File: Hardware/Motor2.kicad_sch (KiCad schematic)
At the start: 36 parts

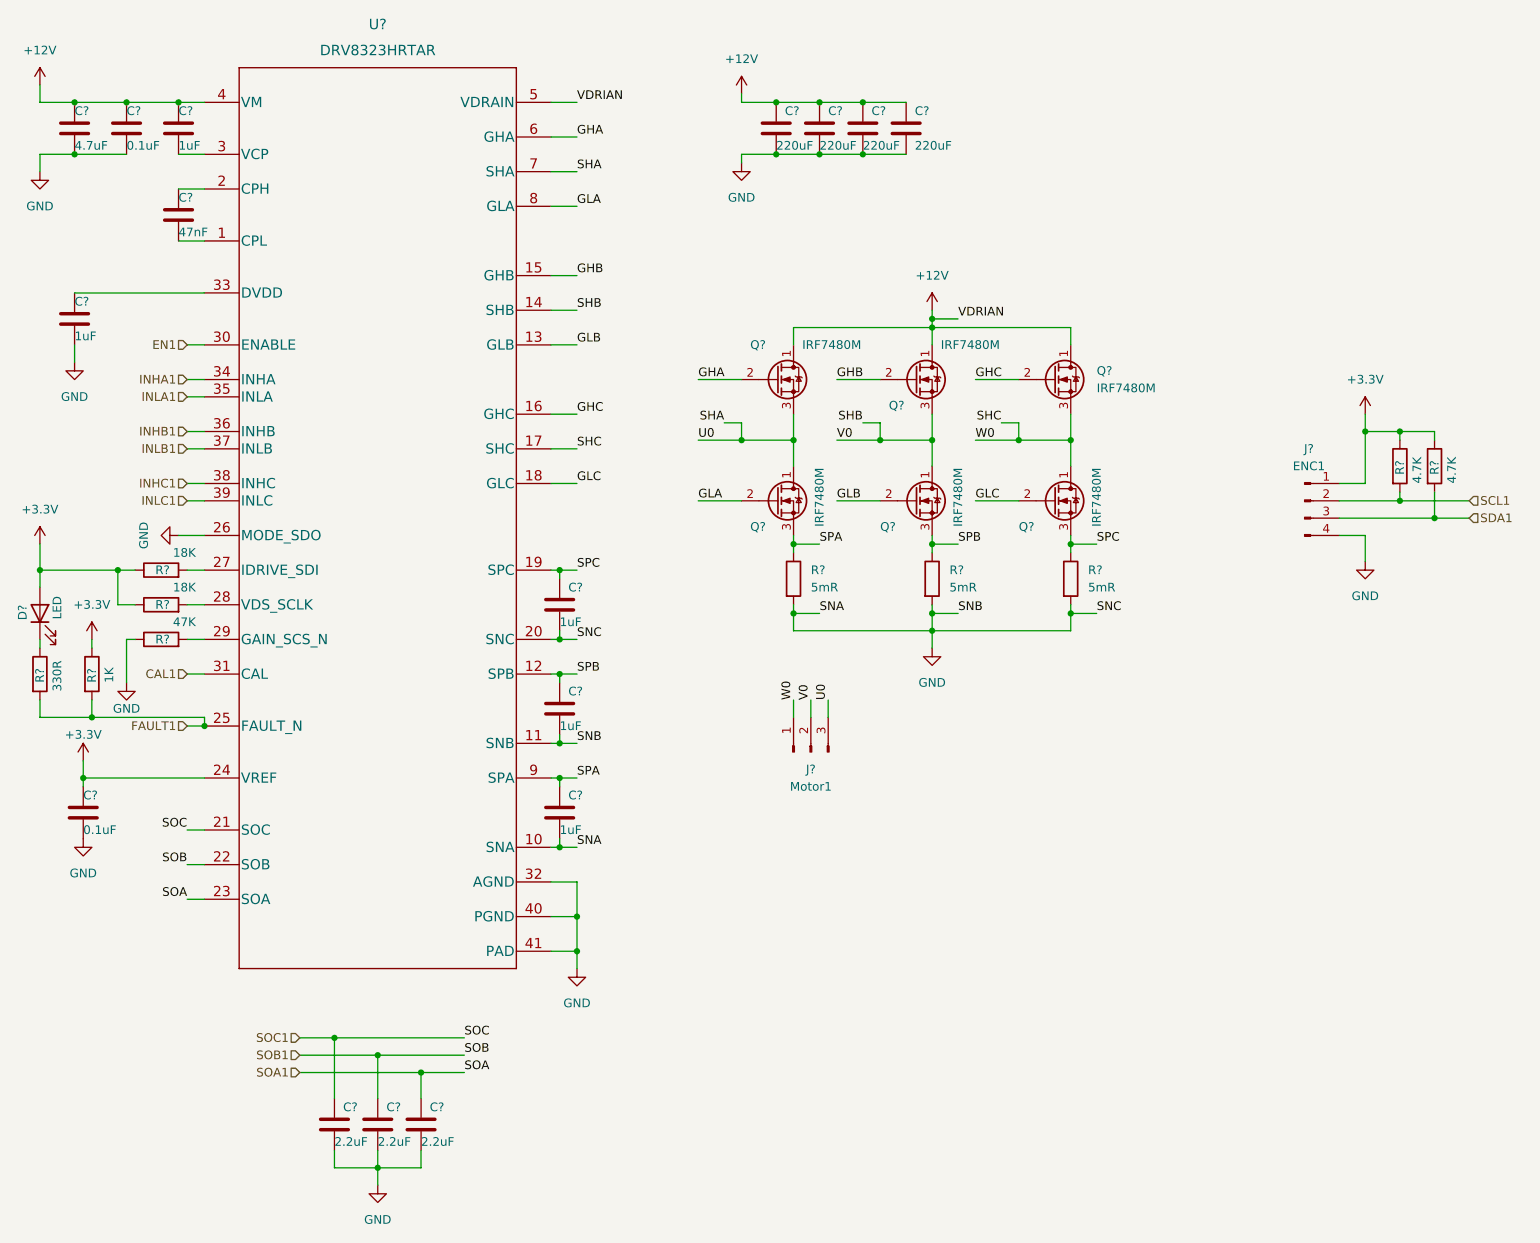
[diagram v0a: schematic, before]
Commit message: Init FreeRTOS
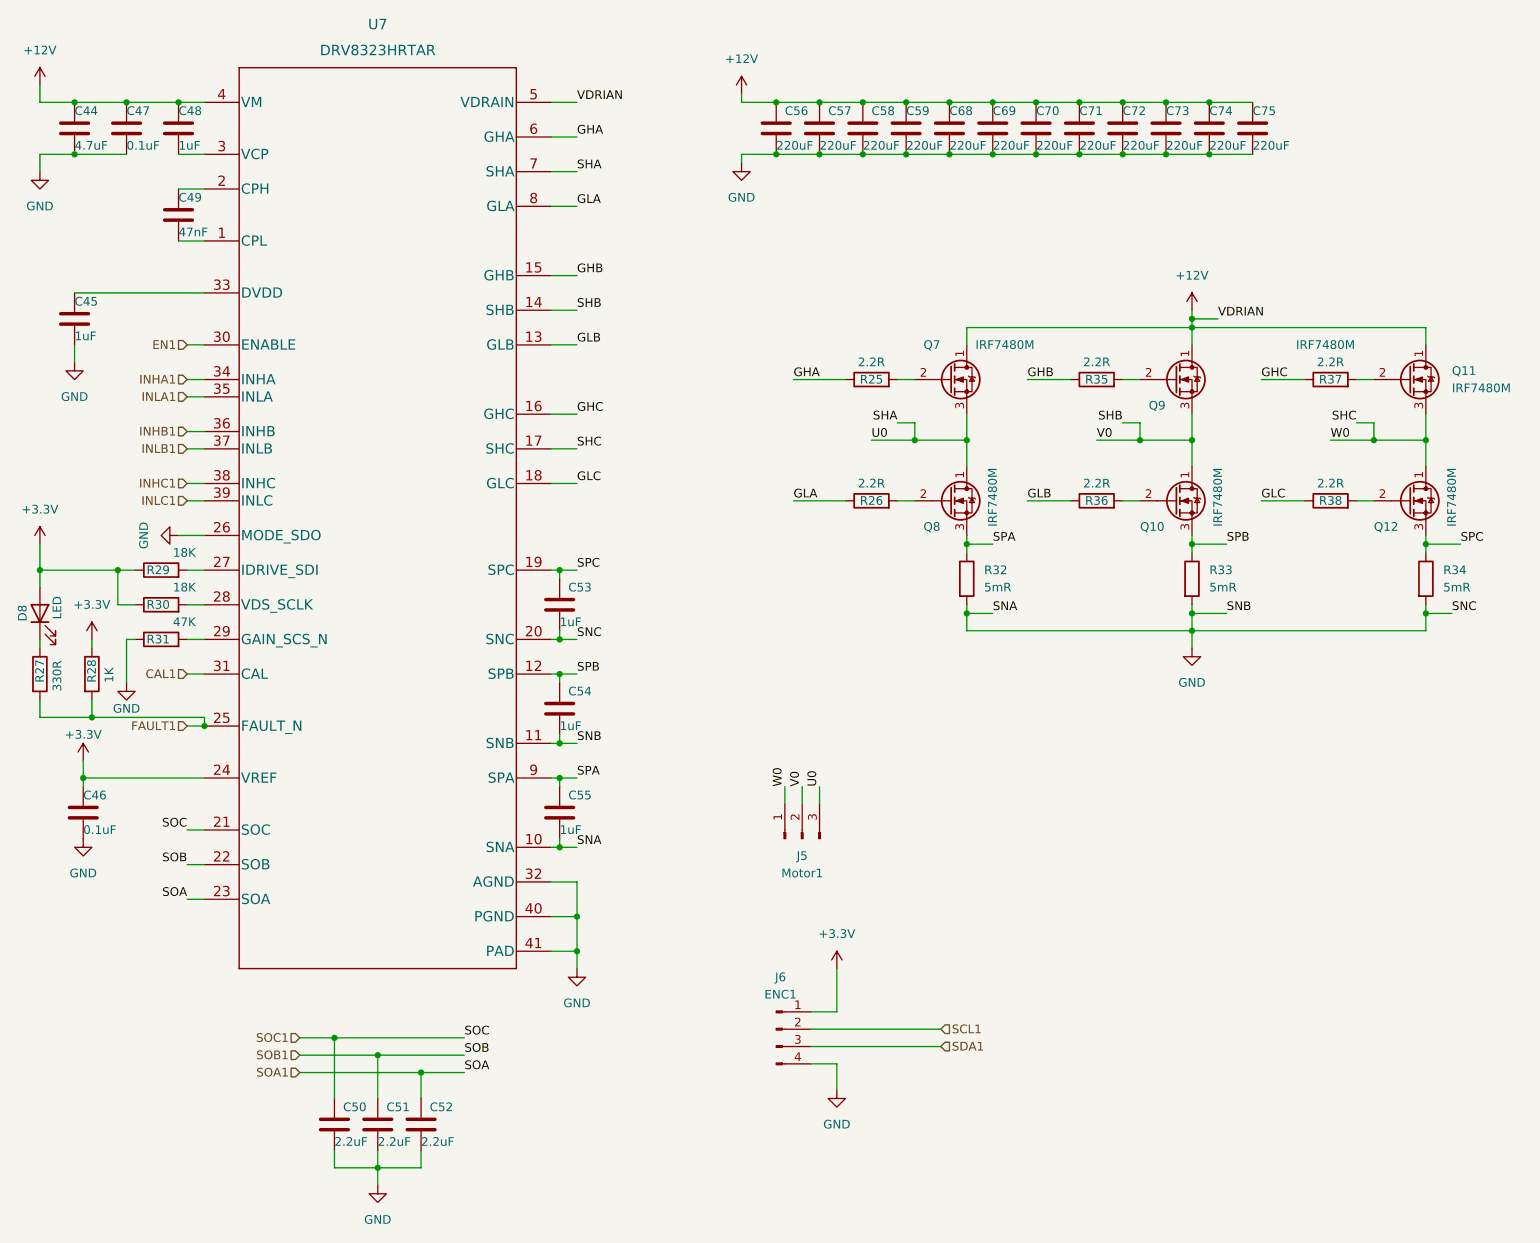
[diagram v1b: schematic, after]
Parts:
- removed R? (x2): 4.7K, Resistor_SMD:R_2512_6332Metric, symbol Device:R
- added C68, C69, C70, C71, C72, C73, C74, C75: 220uF, Capacitor_SMD:C_0805_2012Metric, symbol Device:C
- added R25, R26, R35, R36, R37, R38: 2.2R, Resistor_SMD:R_0402_1005Metric, symbol Device:R
- C50, C51, C52: renamed from C?; footprint (none) -> Capacitor_SMD:C_0402_1005Metric
- C53, C54, C55: renamed from C?; footprint (none) -> Capacitor_SMD:C_0603_1608Metric
- C56, C57, C58, C59: renamed from C?; footprint (none) -> Capacitor_SMD:C_0805_2012Metric
- D8: renamed from D?; footprint LED_SMD:LED_0603_1608Metric -> LED_SMD:LED_0402_1005Metric
- J5: renamed from J?; footprint Connector_AMASS:AMASS_MR30PW-M_1x03_P3.50mm_Horizontal -> Connector_AMASS:MR30_SMD
- J6: renamed from J?; footprint (none) -> Connector_JST:JST_SUR_SM04B-SURS-TF_1x04-1MP_P0.80mm_Horizontal
- gave numbers to parts that had none: 21
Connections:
- net +12V: now also C68.1, C69.1, C70.1, C71.1, C72.1, C73.1, C74.1, C75.1
- net GHA: now also R25.1; no longer Q7.2 (G)
- net GHB: now also R35.1; no longer Q9.2 (G)
- net GHC: now also R37.1; no longer Q11.2 (G)
- net GLA: now also R26.1; no longer Q8.2 (G)
- net GLB: now also R36.1; no longer Q10.2 (G)
- net GLC: now also R38.1; no longer Q12.2 (G)
- net GND: now also C68.2, C69.2, C70.2, C71.2, C72.2, C73.2, C74.2, C75.2
- new net: Q10.2 (G), R36.2
- new net: Q11.2 (G), R37.2
- new net: Q12.2 (G), R38.2
- new net: Q7.2 (G), R25.2
- new net: Q8.2 (G), R26.2
- new net: Q9.2 (G), R35.2
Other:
- moved on the sheet: J5, J6, Q10, Q11, Q12, Q7, Q8, Q9, R32, R33, R34
